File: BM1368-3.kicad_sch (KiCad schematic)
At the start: 39 parts, among them U14 BM1368_mode1, U15 BM1368_mode1

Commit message: DRC Check
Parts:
- removed R52: 10k, Resistor_SMD:R_0805_2012Metric, symbol Device:R
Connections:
- net Net-(U13-VDD1_1) renamed U13-VDD3_1
- net Net-(U13-VDD2_1) renamed U13-VDD2_1
- net Net-(U13-VDD3_1) renamed U13-VDD1_1
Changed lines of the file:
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@@
 	)
 	(junction
+		(at 54.61 50.8)
+		(diameter 0)
+		(color 0 0 0 0)
+	)
+	(junction
 		(at 139.7 55.88)
 		(diameter 0)
@@
 	)
 	(junction
+		(at 67.31 48.26)
+		(diameter 0)
+		(color 0 0 0 0)
+	)
+	(junction
 		(at 234.95 53.34)
 		(diameter 0)
@@
 	)
 	(junction
-		(at 234.95 76.2)
+		(at 78.74 45.72)
 		(diameter 0)
 		(color 0 0 0 0)
 	)
 	(junction
-		(at 97.79 36.83)
+		(at 234.95 76.2)
 		(diameter 0)
 		(color 0 0 0 0)
 	)
 	(junction
-		(at 254 55.88)
+		(at 97.79 36.83)
 		(diameter 0)
 		(color 0 0 0 0)
@@
 	(wire
 		(pts
+			(xy 78.74 45.72) (xy 80.01 45.72)
+		)
+		(stroke
+			(width 0)
+			(type default)
+		)
+	)
+	(wire
+		(pts
 			(xy 260.35 60.96) (xy 260.35 68.58)
 		)
@@
 	(wire
 		(pts
-			(xy 254 55.88) (xy 254 77.47)
-		)
-		(stroke
-			(width 0)
-			(type default)
-		)
-	)
-	(wire
-		(pts
 			(xy 97.79 34.29) (xy 97.79 36.83)
 		)
@@
 	(wire
 		(pts
-			(xy 254 55.88) (xy 274.32 55.88)
+			(xy 232.41 55.88) (xy 274.32 55.88)
 		)
 		(stroke
@@
 	(wire
 		(pts
+			(xy 25.4 50.8) (xy 54.61 50.8)
+		)
+		(stroke
+			(width 0)
+			(type default)
+		)
+	)
+	(wire
+		(pts
 			(xy 195.58 76.2) (xy 196.85 76.2)
 		)
@@
 	(wire
 		(pts
+			(xy 25.4 45.72) (xy 78.74 45.72)
+		)
+		(stroke
+			(width 0)
+			(type default)
+		)
+	)
+	(wire
+		(pts
 			(xy 214.63 36.83) (xy 222.25 36.83)
 		)
@@
 	(wire
 		(pts
-			(xy 78.74 45.72) (xy 80.01 45.72)
+			(xy 139.7 76.2) (xy 139.7 78.74)
 		)
 		(stroke
@@
 	(wire
 		(pts
-			(xy 139.7 76.2) (xy 139.7 78.74)
+			(xy 74.93 78.74) (xy 80.01 78.74)
 		)
 		(stroke
@@
 	(wire
 		(pts
-			(xy 74.93 78.74) (xy 80.01 78.74)
+			(xy 43.18 146.05) (xy 43.18 147.32)
 		)
 		(stroke
@@
 	(wire
 		(pts
-			(xy 43.18 146.05) (xy 43.18 147.32)
+			(xy 232.41 45.72) (xy 234.95 45.72)
 		)
 		(stroke
@@
 	(wire
 		(pts
-			(xy 232.41 45.72) (xy 234.95 45.72)
+			(xy 205.74 36.83) (xy 214.63 36.83)
 		)
 		(stroke
@@
 	(wire
 		(pts
-			(xy 205.74 36.83) (xy 214.63 36.83)
+			(xy 25.4 48.26) (xy 67.31 48.26)
 		)
 		(stroke
@@
 	(wire
 		(pts
-			(xy 254 85.09) (xy 254 87.63)
-		)
-		(stroke
-			(width 0)
-			(type default)
-		)
-	)
-	(wire
-		(pts
 			(xy 67.31 48.26) (xy 80.01 48.26)
 		)
@@
 	(wire
 		(pts
-			(xy 232.41 55.88) (xy 254 55.88)
-		)
-		(stroke
-			(width 0)
-			(type default)
-		)
-	)
-	(wire
-		(pts
 			(xy 60.96 58.42) (xy 80.01 58.42)
 		)
@@
 		)
 	)
-	(label "Net-(U13-VDD3_1)"
-		(at 54.61 50.8 0)
-		(fields_autoplaced yes)
-		(effects
-			(font
-				(size 1.27 1.27)
-			)
-			(justify left bottom)
-		)
-	)
-	(label "Net-(U13-VDD2_1)"
-		(at 67.31 36.83 90)
-		(fields_autoplaced yes)
-		(effects
-			(font
-				(size 1.27 1.27)
-			)
-			(justify left bottom)
-		)
-	)
-	(label "Net-(U13-VDD1_1)"
-		(at 78.74 36.83 90)
-		(fields_autoplaced yes)
-		(effects
-			(font
-				(size 1.27 1.27)
-			)
-			(justify left bottom)
-		)
-	)
 	(hierarchical_label "NRSTO"
 		(shape output)
@@
 		)
 	)
+	(hierarchical_label "U13-VDD1_1"
+		(shape input)
+		(at 25.4 50.8 180)
+		(fields_autoplaced yes)
+		(effects
+			(font
+				(size 1.27 1.27)
+			)
+			(justify right)
+		)
+	)
+	(hierarchical_label "U13-VDD3_1"
+		(shape input)
+		(at 25.4 45.72 180)
+		(fields_autoplaced yes)
+		(effects
+			(font
+				(size 1.27 1.27)
+			)
+			(justify right)
+		)
+	)
 	(hierarchical_label "CLKI"
 		(shape input)
@@
 		)
 	)
+	(hierarchical_label "U13-VDD2_1"
+		(shape input)
+		(at 25.4 48.26 180)
+		(fields_autoplaced yes)
+		(effects
+			(font
+				(size 1.27 1.27)
+			)
+			(justify right)
+		)
+	)
 	(symbol
 		(lib_id "power:+1V2")
@@
 	)
 	(symbol
-		(lib_id "Device:R")
-		(at 254 81.28 0)
-		(unit 1)
-		(exclude_from_sim no)
-		(in_bom yes)
-		(on_board yes)
-		(dnp no)
-		(property "Reference" "R52"
-			(at 251.714 80.772 90)
-			(effects
-				(font
-					(size 1.27 1.27)
-				)
-			)
-		)
-		(property "Value" "10k"
-			(at 255.905 80.645 90)
-			(effects
-				(font
-					(size 1.27 1.27)
-				)
-			)
-		)
-		(property "Footprint" "Resistor_SMD:R_0805_2012Metric"
-			(at 252.222 81.28 90)
-			(effects
-				(font
-					(size 1.27 1.27)
-				)
-				(hide yes)
-			)
-		)
-		(property "Datasheet" "~"
-			(at 254 81.28 0)
-			(effects
-				(font
-					(size 1.27 1.27)
-				)
-				(hide yes)
-			)
-		)
-		(property "Description" ""
-			(at 254 81.28 0)
-			(effects
-				(font
-					(size 1.27 1.27)
-				)
-				(hide yes)
-			)
-		)
-		(pin "1"
-		)
-		(pin "2"
-		)
-		(instances
-			(project "Nerd8"
-				(path "/e63e39d7-6ac0-4ffd-8aa3-1841a4541b55/4cf9c075-d009-4c35-9949-adda70ae20c7/e37fcc16-ab00-4951-a90e-5cb0d9945874"
-					(reference "R52")
-					(unit 1)
-				)
-			)
-		)
-	)
-	(symbol
 		(lib_id "Device:C")
 		(at 60.96 36.83 90)
@@
 					(unit 1)
 				)
-			)
-		)
-	)
-	(symbol
-		(lib_id "power:+1V8")
-		(at 254 87.63 180)
-		(unit 1)
-		(exclude_from_sim no)
-		(in_bom yes)
-		(on_board yes)
-		(dnp no)
-		(property "Reference" "#PWR0366"
-			(at 254 83.82 0)
-			(effects
-				(font
-					(size 1.27 1.27)
-				)
-				(hide yes)
-			)
-		)
-		(property "Value" "GND"
-			(at 254 92.71 90)
-			(effects
-				(font
-					(size 1.27 1.27)
-				)
-			)
-		)
-		(property "Footprint" ""
-			(at 254 87.63 0)
-			(effects
-				(font
-					(size 1.27 1.27)
-				)
-				(hide yes)
-			)
-		)
-		(property "Datasheet" ""
-			(at 254 87.63 0)
-			(effects
-				(font
-					(size 1.27 1.27)
-				)
-				(hide yes)
-			)
-		)
-		(property "Description" ""
-			(at 254 87.63 0)
-			(effects
-				(font
-					(size 1.27 1.27)
-				)
-				(hide yes)
-			)
-		)
-		(pin "1"
-		)
-		(instances
-			(project "Nerd8"
-				(path "/e63e39d7-6ac0-4ffd-8aa3-1841a4541b55/4cf9c075-d009-4c35-9949-adda70ae20c7/e37fcc16-ab00-4951-a90e-5cb0d9945874"
-					(reference "#PWR0366")
-					(unit 1)
-				)

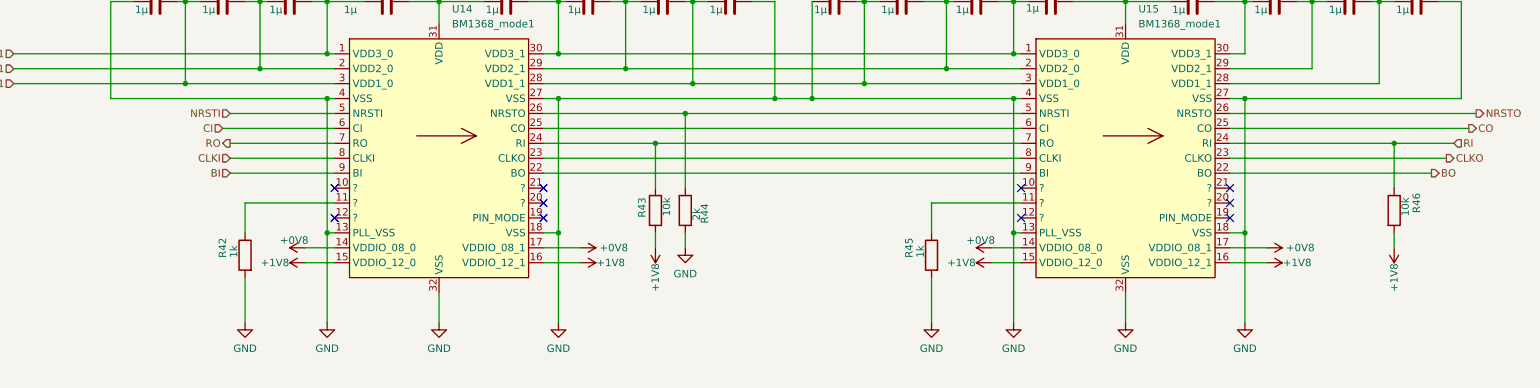
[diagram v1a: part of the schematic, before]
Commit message: References and Logos
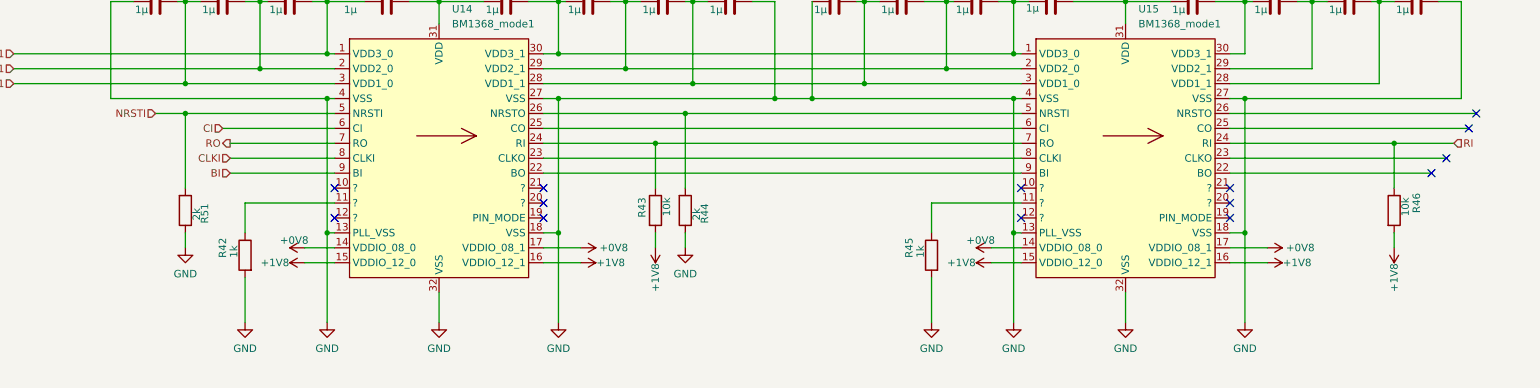
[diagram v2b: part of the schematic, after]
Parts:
- added R51: 2k, Resistor_SMD:R_0805_2012Metric, symbol Device:R
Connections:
- net GND: now also R51.1
- net NRSTI: now also R51.2
- net BO: no longer names the net of U15.22 (BO)
- net CLKO: no longer names the net of U15.23 (CLKO)
- net CO: no longer names the net of U15.25 (CO)
- net NRSTO: no longer names the net of U15.26 (NRSTO)
- no-connect marks 10 -> 14
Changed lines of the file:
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@@
 	)
 	(junction
+		(at 54.61 55.88)
+		(diameter 0)
+		(color 0 0 0 0)
+	)
+	(junction
 		(at 67.31 48.26)
 		(diameter 0)
@@
 	)
 	(no_connect
+		(at 266.7 66.04)
+	)
+	(no_connect
 		(at 196.85 68.58)
 	)
@@
 	)
 	(no_connect
+		(at 269.24 63.5)
+	)
+	(no_connect
 		(at 232.41 73.66)
 	)
@@
 	)
 	(no_connect
+		(at 274.32 55.88)
+	)
+	(no_connect
 		(at 80.01 68.58)
 	)
@@
 	)
 	(no_connect
+		(at 273.05 58.42)
+	)
+	(no_connect
 		(at 232.41 68.58)
 	)
@@
 	(wire
 		(pts
+			(xy 54.61 76.2) (xy 54.61 78.74)
+		)
+		(stroke
+			(width 0)
+			(type default)
+		)
+	)
+	(wire
+		(pts
 			(xy 111.76 146.05) (xy 111.76 147.32)
 		)
@@
 	(wire
 		(pts
+			(xy 54.61 55.88) (xy 54.61 68.58)
+		)
+		(stroke
+			(width 0)
+			(type default)
+		)
+	)
+	(wire
+		(pts
 			(xy 25.4 45.72) (xy 78.74 45.72)
 		)
@@
 	(wire
 		(pts
+			(xy 54.61 55.88) (xy 80.01 55.88)
+		)
+		(stroke
+			(width 0)
+			(type default)
+		)
+	)
+	(wire
+		(pts
 			(xy 78.74 76.2) (xy 80.01 76.2)
 		)
@@
 	(wire
 		(pts
-			(xy 62.23 55.88) (xy 80.01 55.88)
+			(xy 49.53 55.88) (xy 54.61 55.88)
 		)
 		(stroke
@@
 		)
 	)
-	(hierarchical_label "NRSTO"
-		(shape output)
-		(at 274.32 55.88 0)
-		(fields_autoplaced yes)
-		(effects
-			(font
-				(size 1.27 1.27)
-			)
-			(justify left)
-		)
-	)
 	(hierarchical_label "RI"
 		(shape input)
@@
 		)
 	)
-	(hierarchical_label "CLKO"
-		(shape output)
-		(at 269.24 63.5 0)
-		(fields_autoplaced yes)
-		(effects
-			(font
-				(size 1.27 1.27)
-			)
-			(justify left)
-		)
-	)
 	(hierarchical_label "CI"
 		(shape input)
@@
 		)
 	)
-	(hierarchical_label "BO"
-		(shape output)
-		(at 266.7 66.04 0)
-		(fields_autoplaced yes)
-		(effects
-			(font
-				(size 1.27 1.27)
-			)
-			(justify left)
-		)
-	)
-	(hierarchical_label "CO"
-		(shape output)
-		(at 273.05 58.42 0)
-		(fields_autoplaced yes)
-		(effects
-			(font
-				(size 1.27 1.27)
-			)
-			(justify left)
-		)
-	)
 	(hierarchical_label "RO"
 		(shape output)
@@
 	(hierarchical_label "NRSTI"
 		(shape input)
-		(at 62.23 55.88 180)
+		(at 49.53 55.88 180)
 		(fields_autoplaced yes)
 		(effects
@@
 	)
 	(symbol
+		(lib_id "Device:R")
+		(at 54.61 72.39 0)
+		(mirror x)
+		(unit 1)
+		(exclude_from_sim no)
+		(in_bom yes)
+		(on_board yes)
+		(dnp no)
+		(property "Reference" "R51"
+			(at 57.912 72.898 90)
+			(effects
+				(font
+					(size 1.27 1.27)
+				)
+			)
+		)
+		(property "Value" "2k"
+			(at 56.515 73.025 90)
+			(effects
+				(font
+					(size 1.27 1.27)
+				)
+			)
+		)
+		(property "Footprint" "Resistor_SMD:R_0805_2012Metric"
+			(at 52.832 72.39 90)
+			(effects
+				(font
+					(size 1.27 1.27)
+				)
+				(hide yes)
+			)
+		)
+		(property "Datasheet" "~"
+			(at 54.61 72.39 0)
+			(effects
+				(font
+					(size 1.27 1.27)
+				)
+				(hide yes)
+			)
+		)
+		(property "Description" ""
+			(at 54.61 72.39 0)
+			(effects
+				(font
+					(size 1.27 1.27)
+				)
+				(hide yes)
+			)
+		)
+		(pin "1"
+		)
+		(pin "2"
+		)
+		(instances
+			(project "Nerd8"
+				(path "/e63e39d7-6ac0-4ffd-8aa3-1841a4541b55/4cf9c075-d009-4c35-9949-adda70ae20c7/e37fcc16-ab00-4951-a90e-5cb0d9945874"
+					(reference "R51")
+					(unit 1)
+				)
+			)
+		)
+	)
+	(symbol
 		(lib_id "mylib7:+0V8")
 		(at 43.18 137.16 0)
@@
 					(unit 1)
 				)
+			)
+		)
+	)
+	(symbol
+		(lib_id "power:GND")
+		(at 54.61 78.74 0)
+		(mirror y)
+		(unit 1)
+		(exclude_from_sim no)
+		(in_bom yes)
+		(on_board yes)
+		(dnp no)
+		(fields_autoplaced yes)
+		(property "Reference" "#PWR0341"
+			(at 54.61 85.09 0)
+			(effects
+				(font
+					(size 1.27 1.27)
+				)
+				(hide yes)
+			)
+		)
+		(property "Value" "GND"
+			(at 54.61 83.185 0)
+			(effects
+				(font
+					(size 1.27 1.27)
+				)
+			)
+		)
+		(property "Footprint" ""
+			(at 54.61 78.74 0)
+			(effects
+				(font
+					(size 1.27 1.27)
+				)
+				(hide yes)
+			)
+		)
+		(property "Datasheet" ""
+			(at 54.61 78.74 0)
+			(effects
+				(font
+					(size 1.27 1.27)
+				)
+				(hide yes)
+			)
+		)
+		(property "Description" ""
+			(at 54.61 78.74 0)
+			(effects
+				(font
+					(size 1.27 1.27)
+				)
+				(hide yes)
+			)
+		)
+		(pin "1"
+		)
+		(instances
+			(project "Nerd8"
+				(path "/e63e39d7-6ac0-4ffd-8aa3-1841a4541b55/4cf9c075-d009-4c35-9949-adda70ae20c7/e37fcc16-ab00-4951-a90e-5cb0d9945874"
+					(reference "#PWR0341")
+					(unit 1)
+				)
